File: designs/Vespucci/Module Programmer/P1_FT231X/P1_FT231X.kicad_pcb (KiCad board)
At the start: 2 copper layers, 46.2 x 27 mm, 40 parts, among them J1 USB_B_Micro, J2 JTAG Connector, J3 PCIe Connector, J4 Screw_VIn, J5 SWD Header, Q1 AO3400A, Q2 AO3400A, SW1 SW_RST, U1 FT231XS, U2 NL17SZ00, U3 NCP703xN33T, U4 NL17SZ32

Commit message: P1 Programmer Rev A
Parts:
- Q1, Q2: value AO3400A -> SSM3K15AFU; footprint Package_TO_SOT_SMD:SOT-23 -> Package_TO_SOT_SMD:SOT-323_SC-70

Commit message: Update LEDs on P1 3D model
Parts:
- D1, D2, D3, D4, D5, D6, D7: footprint Diode_SMD:D_0603_1608Metric -> LED_SMD:LED_0603_1608Metric
- Q1, Q2: value SSM3K15AFU -> BSS138W

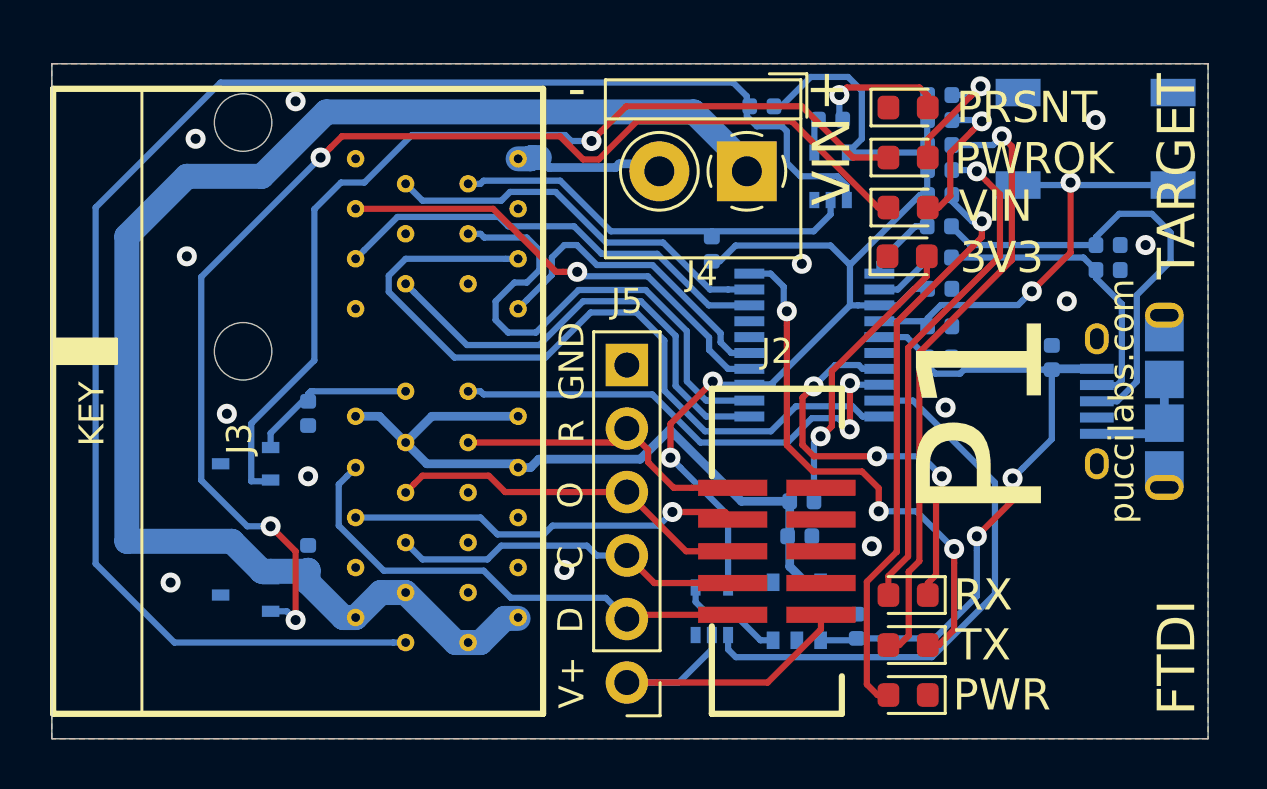
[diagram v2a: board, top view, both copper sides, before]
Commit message: Update P1 Rev B, R1 Rev B, D1 Rev A
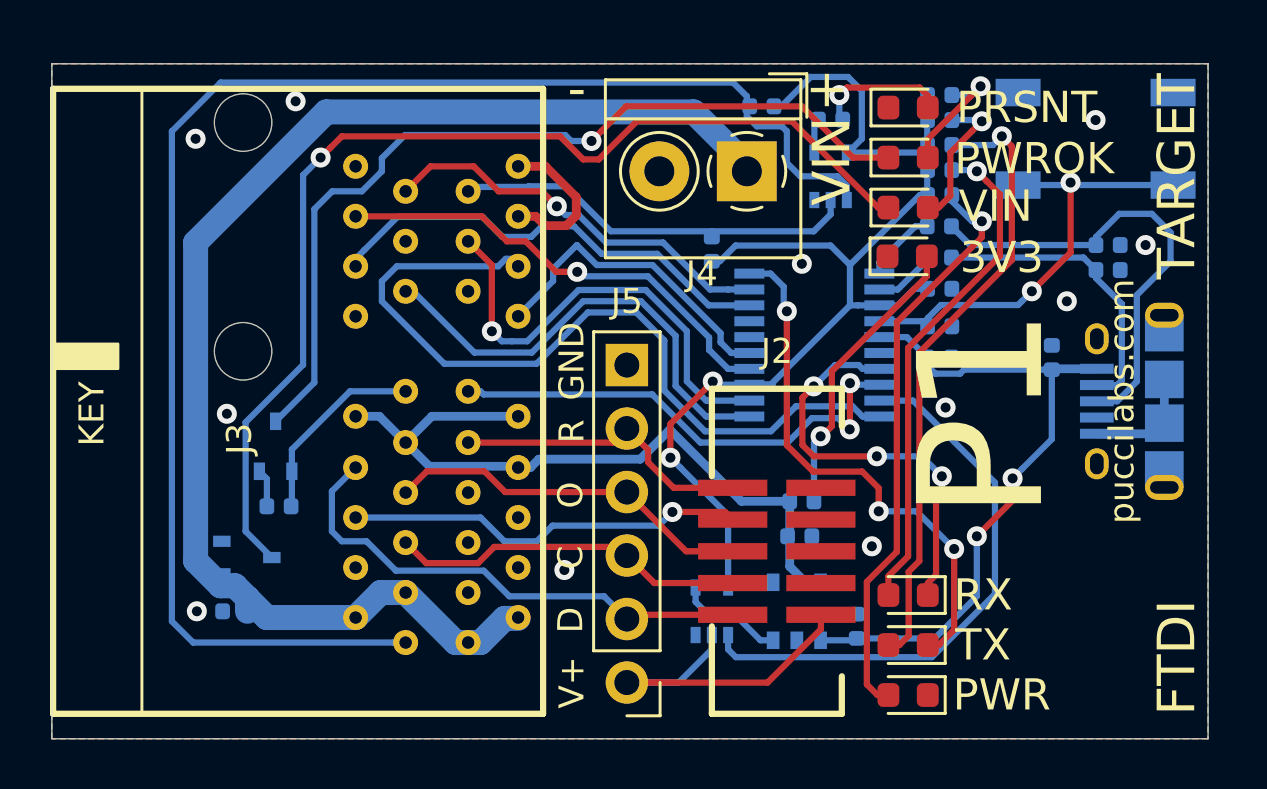
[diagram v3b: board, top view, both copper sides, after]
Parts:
- D1: value TX -> LED
- D2: value FTDI_3V3 -> LED
- D3: value RX -> LED
- D4: value TARGET_3V3 -> LED
- D5: value TARGET_VIN -> LED
- D6: value TARGET_POWEROK -> LED
- D7: value TARGET_PRESENT -> LED
- moved R10 3.89 mm to (125.1, 104.2), turned to 180 degrees
- moved R8 3.64 mm to (123.3, 108.4), turned to 180 degrees
- moved Q1 1.50 mm to (123.8, 106.2), turned to 0 degrees
- moved Q2 1.39 mm to (125.0, 101.8), turned to 90 degrees
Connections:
- Q1 pad 2: Net-(D5-Pad1) -> GND
- Q1 pad 3: GND -> Net-(D5-Pad1)
- Q2 pad 2: Net-(D6-Pad1) -> GND
- Q2 pad 3: GND -> Net-(D6-Pad1)
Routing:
- net Net-(D5-Pad1): track 49.2 -> 43.2 mm, vias 3 -> 1
- net +BATT: track 58.7 -> 53.8 mm
- net Net-(D6-Pad1): track 38.4 -> 35.2 mm
- net /PRSNT1: track 63.6 -> 60.6 mm
- net /hRTS: track 21.0 -> 18.3 mm, vias 0 -> 1
- net GND: track 10.5 -> 12.4 mm, vias 13 -> 11
- net /hTX: track 31.3 -> 32.1 mm
- net /PWR_OK: track 7.13 -> 7.80 mm
- net /TMS: track 20.0 -> 20.5 mm
- net /hCTS: track 15.8 -> 16.2 mm, vias 0 -> 1
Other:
- board text added: "P1 Module Programmer/Debugger Puccinelli Laboratories 20200523 REV B"
- board text removed: "P1 Module Programmer/Debugger Puccinelli Laboratories 20200516 REV A"

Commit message: R4R: P1 Rev B, R1 Rev B
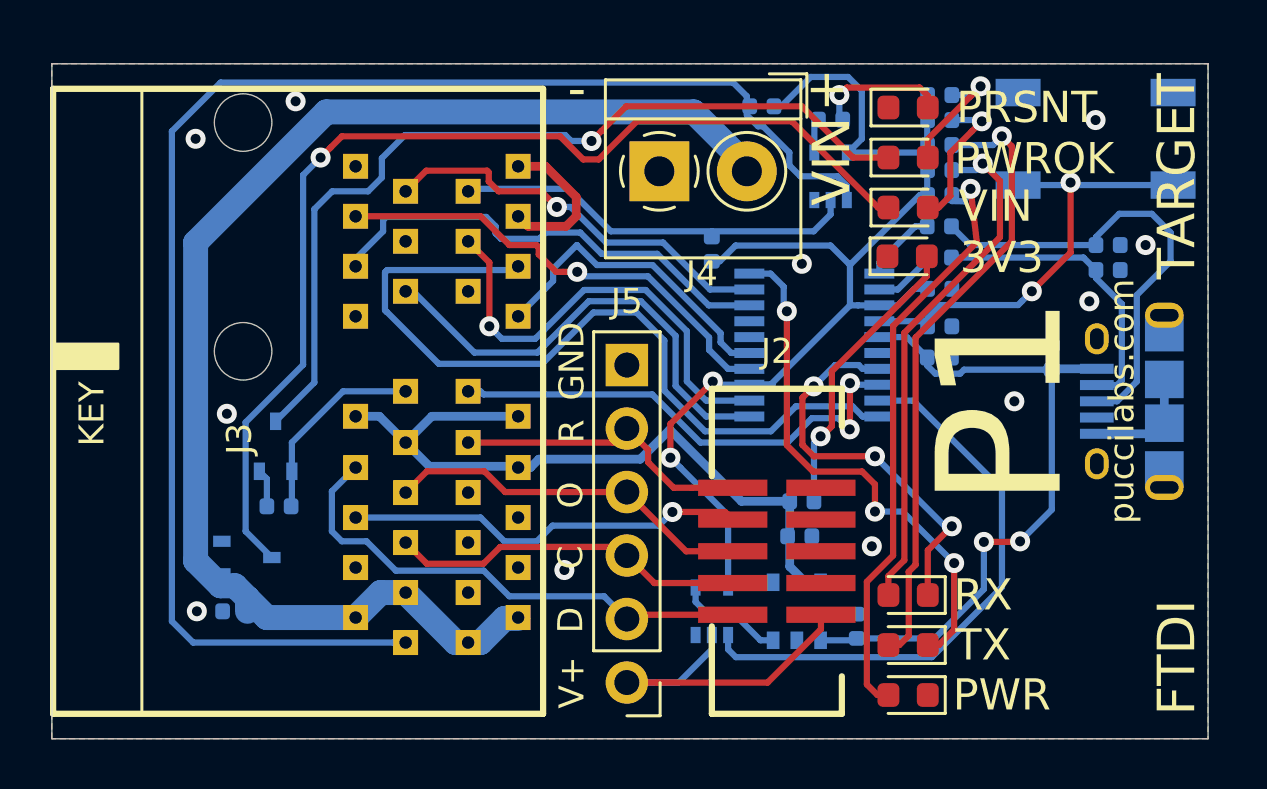
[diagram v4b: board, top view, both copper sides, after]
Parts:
- added G1: OSHW_logo, Custom_Footprints:OSHW_logo, B.Cu at (158.0, 109.5)
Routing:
- net +5V: track 27.1 -> 27.9 mm
- net Net-(D2-Pad2): track 23.2 -> 24.0 mm
- net /LED_RX: track 16.6 -> 16.0 mm
- net Net-(D3-Pad2): track 20.2 -> 20.7 mm
